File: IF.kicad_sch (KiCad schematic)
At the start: 30 parts, among them J1 LINE_IN, K1 RS-12, Q2 DTC143Z, U5 MC33079

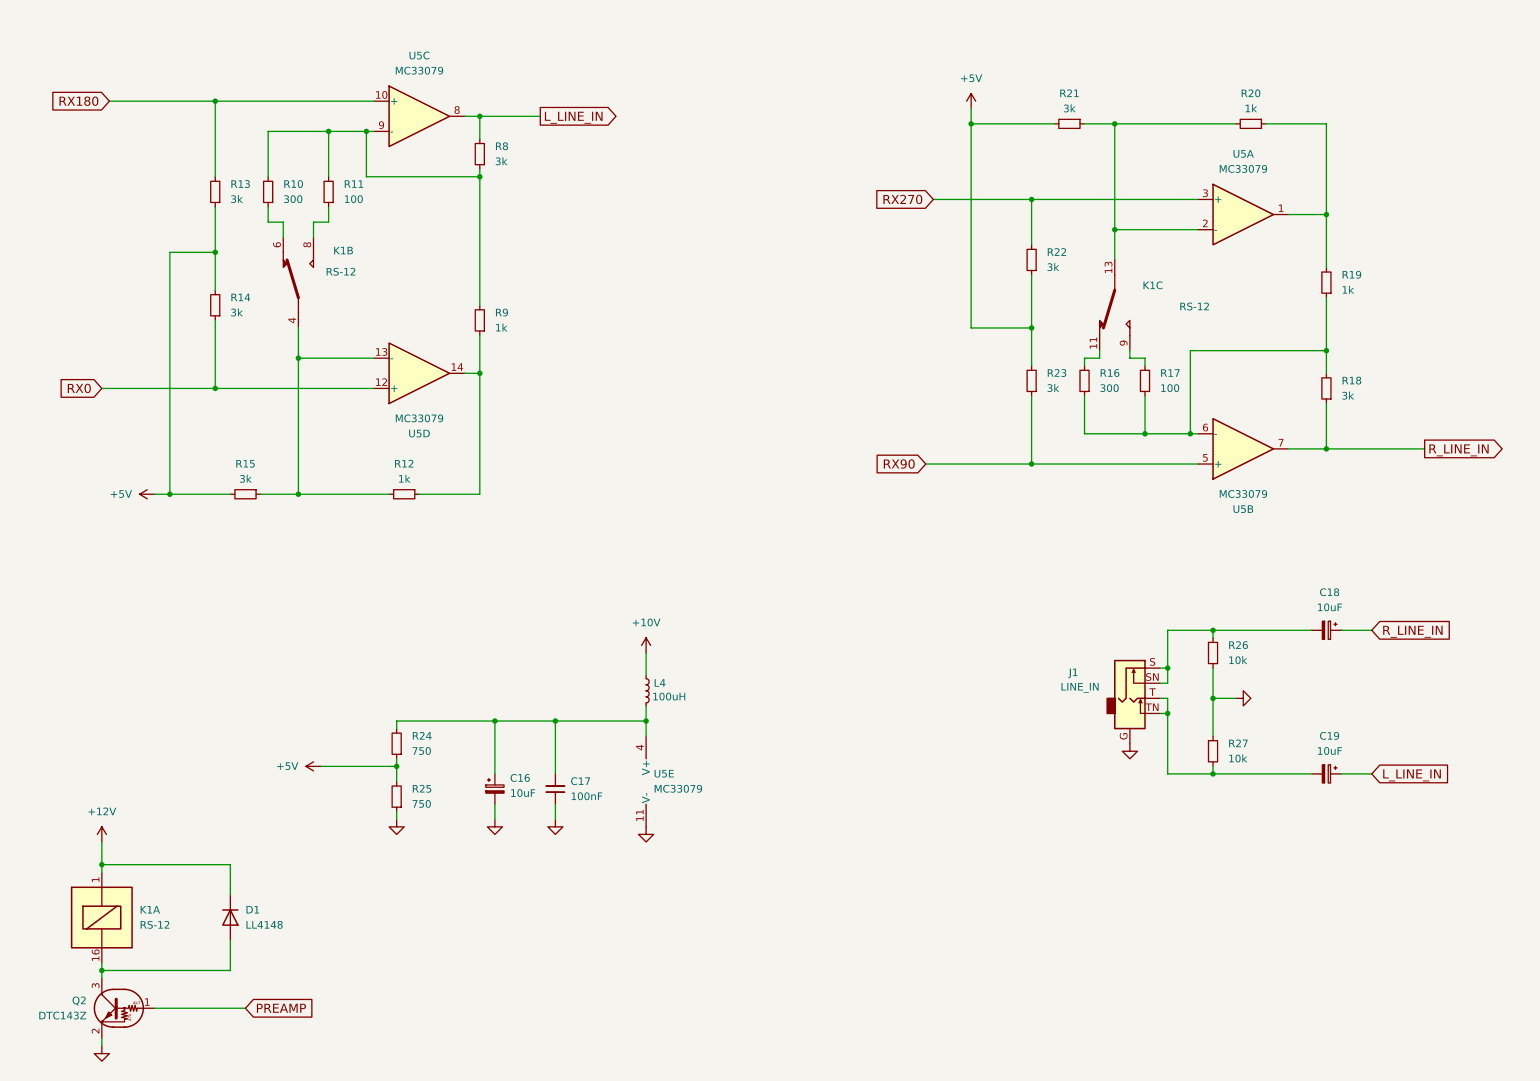
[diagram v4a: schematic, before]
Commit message: progress in PCB, schematics some footprints are still missing
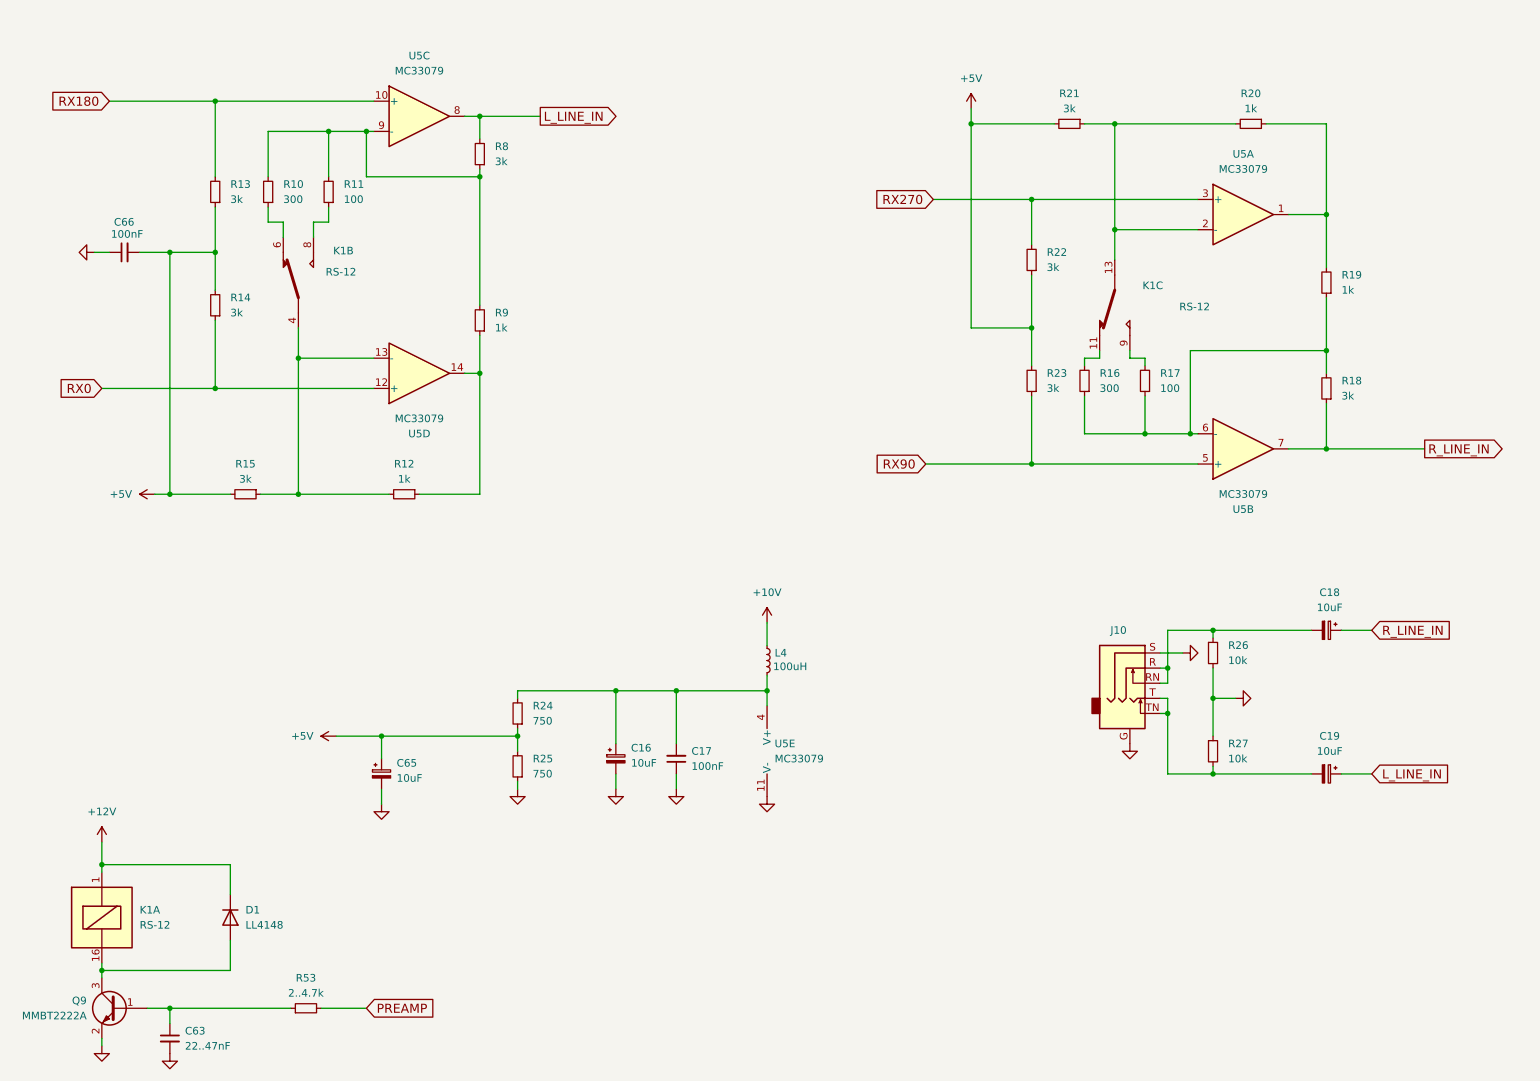
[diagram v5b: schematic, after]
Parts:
- removed J1: LINE_IN, Connector_Audio:Jack_3.5mm_CUI_SJ1-3525N_Horizontal, symbol Connector_Audio:AudioJack2_Ground_Switch
- removed Q2: DTC143Z, Package_TO_SOT_SMD:SOT-523, symbol Transistor_BJT:DTC143Z
- added C63: 22..47nF, SDR_footprints:C_1206_0603, symbol Device:C_Small
- added C65: 10uF, Capacitor_Tantalum_SMD:CP_EIA-3216-18_Kemet-A_Pad1.58x1.35mm_HandSolder, symbol Device:C_Polarized_Small
- added C66: 100nF, SDR_footprints:C_1206_0603, symbol Device:C_Small
- added J10: AudioJack3_Ground_SwitchTR, Connector_Audio:Jack_3.5mm_CUI_SJ1-3525N_Horizontal, symbol Connector_Audio:AudioJack3_Ground_SwitchTR
- added Q9: MMBT2222A, Package_TO_SOT_SMD:SOT-23, symbol Transistor_BJT:MMBT2222A
- added R53: 2..4.7k, SDR_footprints:R_1206_0603, symbol Device:R_Small
- C17: footprint Capacitor_SMD:C_0603_1608Metric_Pad1.08x0.95mm_HandSolder -> SDR_footprints:C_1206_0603
- R24, R25: footprint Resistor_SMD:R_0603_1608Metric_Pad0.98x0.95mm_HandSolder -> SDR_footprints:R_1206_0603
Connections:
- net +5V: now also C65.1, C66.2
- net GND: now also C63.2, C65.2, C66.1, J10.G, J10.S, Q9.2 (E)
- net PREAMP: now also R53.2
- net at D1.2 (A), K1.16: now also Q9.3 (C)
- net at C19.2, R27.2: now also J10.T, J10.TN
- net at C18.2, R26.1: now also J10.R, J10.RN
- new net: C63.1, Q9.1 (B), R53.1
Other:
- moved on the sheet: C16, C17, L4, R24, R25, U5E

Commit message: progress on PCB
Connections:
- net at R10.2, R8.1, R9.2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: now also R11.1; no longer R11.2
- net at K1.8: now also R11.2; no longer R11.1
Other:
- moved on the sheet: R11
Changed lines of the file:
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@@
 	(symbol
 		(lib_id "Device:R_Small")
-		(at 78.74 45.72 180)
+		(at 78.74 45.72 0)
 		(unit 1)
 		(exclude_from_sim no)
@@
 					(size 1.27 1.27)
 				)
-				(justify right)
+				(justify left)
 			)
 		)
@@
 					(size 1.27 1.27)
 				)
-				(justify right)
+				(justify left)
 			)
 		)
